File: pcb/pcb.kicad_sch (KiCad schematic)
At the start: 50 parts, among them J1 Conn_01x02_Pin, J2 BAT, SW1 SW_SPST, SW10 SW_SPST, SW11 SW_SPST, SW12 SW_SPST, SW13 SW_SPST, SW14 SW_SPST, SW15 SW_SPST, SW16 SW_SPST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

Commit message: вырез
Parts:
- removed J1: Conn_01x02_Pin, Two:Battery, symbol Two:Conn_01x02_Pin
- removed J2: BAT, Two:JST_SH_Battery_DUAL, symbol Two:Conn_01x02_Pin
- added BT1: Battery, symbol Device:Battery
- added H5: BAT-, symbol Mechanical:MountingHole_Pad
- added H6: BAT+, symbol Mechanical:MountingHole_Pad
- U1: footprint Two:XIAO_nRF52840_DUAL -> Two:XIAO_nRF52840_DUAL_WINDOW
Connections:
- net B+: now also H6.1; no longer U1.19 (BAT+)
- net B-: now also BT1.2 (-), H5.1; no longer U1.20 (BAT-)
- net at PWR1.2 (B): now also BT1.1 (+)
- net +3V3: no longer names the net of U1.12 (3V3)
- net +5V: no longer names the net of U1.14 (5V)
- no-connect marks 2 -> 6

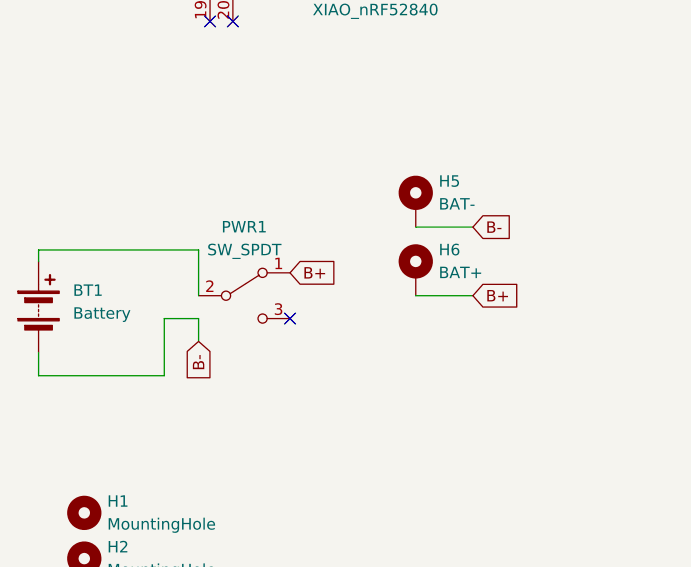
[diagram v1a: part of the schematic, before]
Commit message: расширил вырез
и добавил пады питания
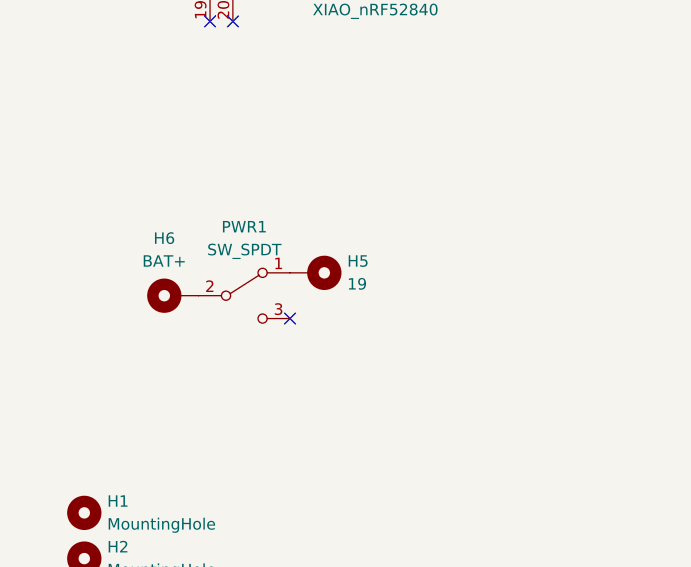
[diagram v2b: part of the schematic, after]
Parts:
- removed BT1: Battery, symbol Device:Battery
- H5: value BAT- -> 19; footprint (none) -> TestPoint:TestPoint_THTPad_1.0x1.0mm_Drill0.5mm
- H6: footprint (none) -> TestPoint:TestPoint_THTPad_1.0x1.0mm_Drill0.5mm
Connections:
- net B- is gone; now on an unnamed net: H5.1
- net at PWR1.2 (B): now also H6.1
- net B+: no longer names the net of PWR1.1 (A)
- net B+: no longer H6.1
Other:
- moved on the sheet: H5, H6

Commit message: добавил батарейку
и разъём с другой стороны
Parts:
- added BT1: LP601730, Two:lp601730, symbol Device:Battery_Cell
- added J1: Conn_01x02_Pin, Two:JST_SH_Battery_DUAL_, symbol Two:Conn_01x02_Pin
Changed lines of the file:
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@@
+	)
+	(symbol
+		(lib_id "Two:Conn_01x02_Pin")
+		(at 38.1 99.06 0)
+		(unit 1)
+		(exclude_from_sim no)
+		(in_bom yes)
+		(on_board yes)
+		(dnp no)
+		(fields_autoplaced yes)
+		(property "Reference" "J1"
+			(at 38.735 93.98 0)
+			(effects
+				(font
+					(size 1.27 1.27)
+				)
+			)
+		)
+		(property "Value" "Conn_01x02_Pin"
+			(at 38.735 96.52 0)
+			(effects
+				(font
+					(size 1.27 1.27)
+				)
+			)
+		)
+		(property "Footprint" "Two:JST_SH_Battery_DUAL_"
+			(at 38.1 99.06 0)
+			(effects
+				(font
+					(size 1.27 1.27)
+				)
+				(hide yes)
+			)
+		)
+		(property "Datasheet" "~"
+			(at 38.1 99.06 0)
+			(effects
+				(font
+					(size 1.27 1.27)
+				)
+				(hide yes)
+			)
+		)
+		(property "Description" "Generic connector, single row, 01x02, script generated"
+			(at 38.1 99.06 0)
+			(effects
+				(font
+					(size 1.27 1.27)
+				)
+				(hide yes)
+			)
+		)
+		(pin "2"
+		)
+		(pin "1"
+		)
+		(instances
+			(project ""
+				(path "/1fd8269d-bfbb-4294-b901-abae7a95debd"
+					(reference "J1")
+					(unit 1)
+				)
+			)
+		)
 	)
 	(symbol
@@
 					(unit 1)
 				)
+			)
+		)
+	)
+	(symbol
+		(lib_id "Device:Battery_Cell")
+		(at 60.96 105.41 0)
+		(unit 1)
+		(exclude_from_sim no)
+		(in_bom yes)
+		(on_board yes)
+		(dnp no)
+		(fields_autoplaced yes)
+		(property "Reference" "BT1"
+			(at 64.77 102.2984 0)
+			(effects
+				(font
+					(size 1.27 1.27)
+				)
+				(justify left)
+			)
+		)
+		(property "Value" "LP601730"
+			(at 64.77 104.8384 0)
+			(effects
+				(font
+					(size 1.27 1.27)
+				)
+				(justify left)
+			)
+		)
+		(property "Footprint" "Two:lp601730"
+			(at 60.96 103.886 90)
+			(effects
+				(font
+					(size 1.27 1.27)
+				)
+				(hide yes)
+			)
+		)
+		(property "Datasheet" "~"
+			(at 60.96 103.886 90)
+			(effects
+				(font
+					(size 1.27 1.27)
+				)
+				(hide yes)
+			)
+		)
+		(property "Description" "Single-cell battery"
+			(at 60.96 105.41 0)
+			(effects
+				(font
+					(size 1.27 1.27)
+				)
+				(hide yes)
+			)
+		)
+		(pin "1"
+		)
+		(pin "2"
+		)
+		(instances
+			(project ""
+				(path "/1fd8269d-bfbb-4294-b901-abae7a95debd"
+					(reference "BT1")
+					(unit 1)
+				)

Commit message: in progress
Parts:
- removed H5: 19, TestPoint:TestPoint_THTPad_1.0x1.0mm_Drill0.5mm, symbol Mechanical:MountingHole_Pad
- removed H6: BAT+, TestPoint:TestPoint_THTPad_1.0x1.0mm_Drill0.5mm, symbol Mechanical:MountingHole_Pad
- removed J1: Conn_01x02_Pin, Two:JST_SH_Battery_DUAL_, symbol Two:Conn_01x02_Pin
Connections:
- net at PWR1.1 (A): now also U1.19 (BAT+)
- net at PWR1.2 (B): now also BT1.1 (+)
- net at U1.20 (BAT-): now also BT1.2 (-)
- no-connect marks 6 -> 4
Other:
- moved on the sheet: BT1, PWR1

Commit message: провода нарисовал
Размеры поправил
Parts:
- U1: footprint Two:XIAO_nRF52840_DUAL_WINDOW -> Two:XIAO_nRF52840_DUAL_WINDOW_NO_CAP
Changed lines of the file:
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@@
 			)
 		)
-		(property "Footprint" "Two:XIAO_nRF52840_DUAL_WINDOW"
+		(property "Footprint" "Two:XIAO_nRF52840_DUAL_WINDOW_NO_CAP"
 			(at 46.99 39.37 0)
 			(effects
